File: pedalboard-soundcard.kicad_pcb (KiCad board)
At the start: 2 copper layers, 65 x 56 mm, 76 parts, among them J1 RPi_GPIO, J2 Conn_02x03_Odd_Even, J3 Conn_02x03_Odd_Even, U1 AT24CS01-STUM, U2 ncp163, U3 ncp163, U4 PCM1863DBT, U5 ncp163, U6 PCM5242RHBR, X1 22.5792Mhz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

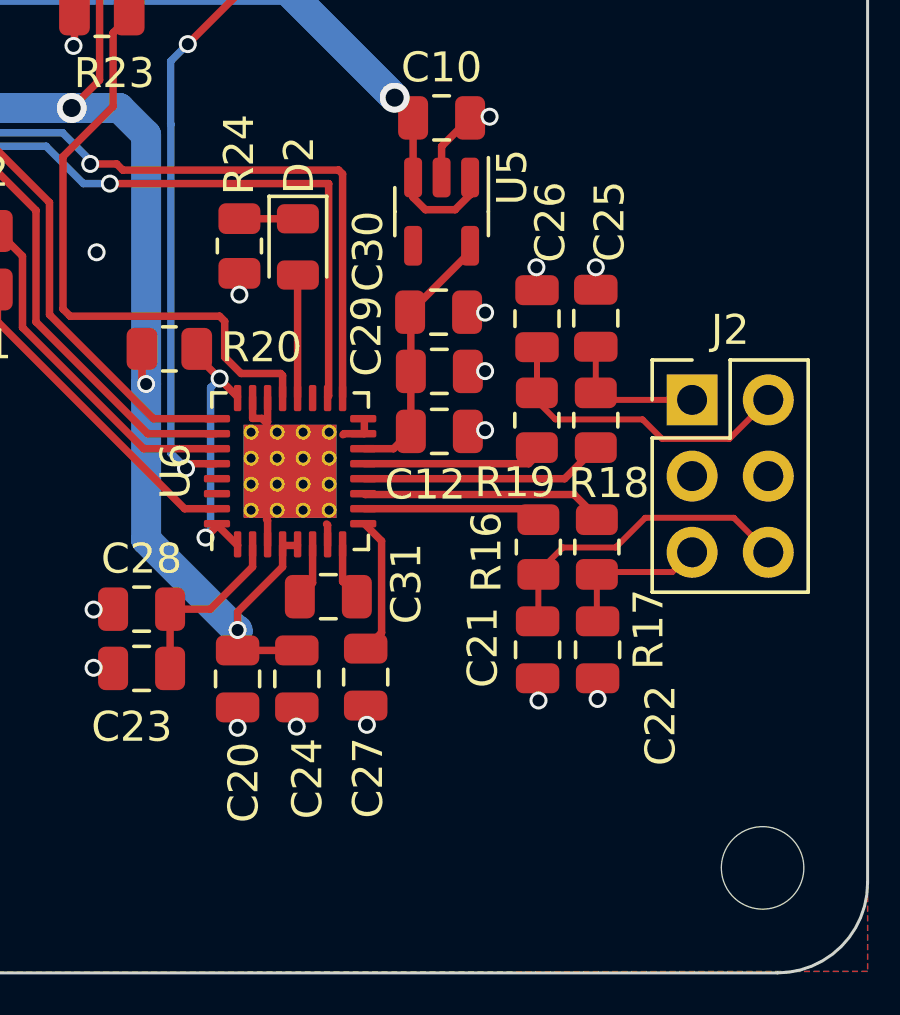
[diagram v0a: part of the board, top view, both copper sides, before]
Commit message: Cleanup silkscreen
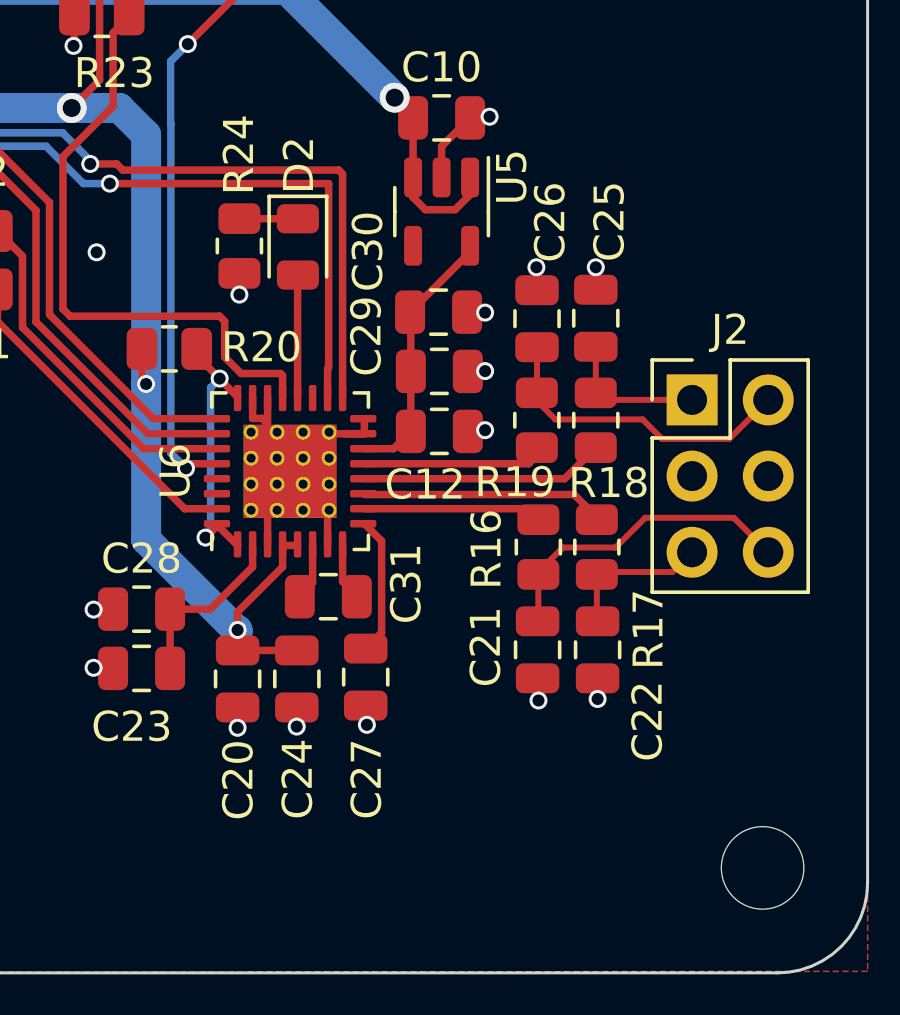
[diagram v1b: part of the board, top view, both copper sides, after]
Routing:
- net GND: track 56.3 -> 62.8 mm
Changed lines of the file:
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@@
     (property "ki_keywords" "mounting hole")
     (attr through_hole)
-    (fp_text reference "H4" (at 0 -4.0005) (layer "F.SilkS") hide
+    (fp_text reference "H4" (at 1.63 4.79) (layer "F.SilkS") hide
         (effects (font (size 1 1) (thickness 0.15)))
     )
@@
     (property "ki_keywords" "cap capacitor")
     (attr smd)
-    (fp_text reference "C21" (at -0.08 1.825 90) (layer "F.SilkS")
+    (fp_text reference "C21" (at -0.1 1.72 90) (layer "F.SilkS")
         (effects (font (size 1 1) (thickness 0.15)))
     )
@@
     (property "ki_keywords" "R res resistor")
     (attr smd)
-    (fp_text reference "R16" (at 0.17 1.725 90) (layer "F.SilkS")
+    (fp_text reference "R16" (at 0.075 1.725 90) (layer "F.SilkS")
         (effects (font (size 1 1) (thickness 0.15)))
     )
@@
     (property "ki_keywords" "cap capacitor")
     (attr smd)
-    (fp_text reference "C24" (at -3.325 0.35 90) (layer "F.SilkS")
+    (fp_text reference "C24" (at -3.34 0.035 90) (layer "F.SilkS")
         (effects (font (size 1 1) (thickness 0.15)))
     )
@@
     (property "ki_keywords" "cap capacitor")
     (attr smd)
-    (fp_text reference "C22" (at 2.52 -2.1 90) (layer "F.SilkS")
+    (fp_text reference "C22" (at 2.38 -1.67 90) (layer "F.SilkS")
         (effects (font (size 1 1) (thickness 0.15)))
     )
@@
     (property "ki_keywords" "cap capacitor")
     (attr smd)
-    (fp_text reference "C27" (at -3.36 0.08 90) (layer "F.SilkS")
+    (fp_text reference "C27" (at -3.4 0.04 90) (layer "F.SilkS")
         (effects (font (size 1 1) (thickness 0.15)))
     )
@@
     (property "ki_keywords" "cap capacitor")
     (attr smd)
-    (fp_text reference "C20" (at -3.45 0.2 90) (layer "F.SilkS")
+    (fp_text reference "C20" (at -3.37 0.03 90) (layer "F.SilkS")
         (effects (font (size 1 1) (thickness 0.15)))
     )
@@
   )
   (segment (start 66.650001 81.749999) (end 66.65 81.75) (width 0.25) (layer "F.Cu") (net 2))
+  (segment (start 93.499999 94.251999) (end 93.499999 92.527001) (width 0.25) (layer "F.Cu") (net 2))
   (segment (start 66.650001 79.249999) (end 66.65 79.25) (width 0.25) (layer "F.Cu") (net 2))
   (segment (start 88.35 96.375) (end 87.715 96.375) (width 0.25) (layer "F.Cu") (net 2))
@@
   (segment (start 96.724999 90.026559) (end 96.724999 90.526685) (width 0.25) (layer "F.Cu") (net 2))
   (segment (start 104.5 98.68) (end 104.5 99.37) (width 0.25) (layer "F.Cu") (net 2))
-  (segment (start 95.5 94.251999) (end 95.5 93.572099) (width 0.25) (layer "F.Cu") (net 2))
   (segment (start 82.84 61.15) (end 83.07 60.92) (width 0.25) (layer "F.Cu") (net 2))
   (segment (start 100.86 80) (end 100.9 79.96) (width 0.25) (layer "F.Cu") (net 2))
@@
   (segment (start 82.85 61.825) (end 82.85 61.16) (width 0.25) (layer "F.Cu") (net 2))
   (segment (start 67.4 61.725) (end 66.35 60.675) (width 0.25) (layer "F.Cu") (net 2))
-  (segment (start 95.5 93.572099) (end 95.465001 93.5371) (width 0.25) (layer "F.Cu") (net 2))
   (segment (start 94.475 100.285) (end 94.47 100.29) (width 0.01) (layer "F.Cu") (net 2))
   (segment (start 73.95 75.4) (end 73.95 74.65) (width 0.25) (layer "F.Cu") (net 2))
   (segment (start 93.4626 90.17077) (end 93.499999 90.133371) (width 0.25) (layer "F.Cu") (net 2))
-  (segment (start 93.499999 94.251999) (end 93.499999 93.420629) (width 0.25) (layer "F.Cu") (net 2))
   (segment (start 87.715 96.375) (end 87.7 96.39) (width 0.25) (layer "F.Cu") (net 2))
   (segment (start 100.175 90.45) (end 100.71 90.45) (width 0.25) (layer "F.Cu") (net 2))
@@
   (segment (start 100.74 88.45) (end 100.75 88.44) (width 0.25) (layer "F.Cu") (net 2))
   (segment (start 96.81 100.23) (end 96.77 100.19) (width 0.25) (layer "F.Cu") (net 2))
-  (segment (start 96.045226 90.526685) (end 96.0101 90.561811) (width 0.25) (layer "F.Cu") (net 2))
   (segment (start 62.150052 82.250001) (end 63.5 82.25) (width 0.25) (layer "F.Cu") (net 2))
   (segment (start 96.724999 90.526685) (end 96.045226 90.526685) (width 0.25) (layer "F.Cu") (net 2))
+  (segment (start 96.6875 90.527) (end 95.5 90.527) (width 0.25) (layer "F.Cu") (net 2))
   (segment (start 59.3925 77.0175) (end 59.42 76.99) (width 0.25) (layer "F.Cu") (net 2))
   (segment (start 102.46 84.98) (end 102.48 85) (width 0.25) (layer "F.Cu") (net 2))
@@
   (segment (start 88.75 72.62) (end 88.75 73.15) (width 0.25) (layer "F.Cu") (net 2))
   (segment (start 71.475 97.525) (end 71.47 97.53) (width 0.25) (layer "F.Cu") (net 2))
+  (segment (start 93.499999 92.527001) (end 94.25 91.777) (width 0.25) (layer "F.Cu") (net 2))
   (segment (start 63.349999 80.750001) (end 62.150052 80.750001) (width 0.25) (layer "F.Cu") (net 2))
   (segment (start 100.175 88.45) (end 100.74 88.45) (width 0.25) (layer "F.Cu") (net 2))
@@
   (segment (start 64.3 74.35) (end 64.3 73.65) (width 0.25) (layer "F.Cu") (net 2))
   (segment (start 100.15 86.475) (end 100.735 86.475) (width 0.25) (layer "F.Cu") (net 2))
+  (segment (start 95.5 93.027) (end 94.683333 92.210333) (width 0.25) (layer "F.Cu") (net 2))
   (segment (start 86.04 61.245001) (end 86.04 62.4775) (width 0.25) (layer "F.Cu") (net 2))
   (segment (start 87.1375 63.575) (end 87.1375 64.4225) (width 0.25) (layer "F.Cu") (net 2))
@@
   (segment (start 100.735 86.475) (end 100.75 86.49) (width 0.25) (layer "F.Cu") (net 2))
   (segment (start 58.1 96.7625) (end 58.1 97.46) (width 0.25) (layer "F.Cu") (net 2))
+  (segment (start 95.5 94.251999) (end 95.5 93.027) (width 0.25) (layer "F.Cu") (net 2))
   (segment (start 86.04 62.4775) (end 87.1375 63.575) (width 0.25) (layer "F.Cu") (net 2))
   (segment (start 94.475 99.65) (end 94.475 100.285) (width 0.01) (layer "F.Cu") (net 2))
@@
   (segment (start 63.5 82.75) (end 62.150052 82.75) (width 0.25) (layer "F.Cu") (net 2))
   (segment (start 102.48 85) (end 102.48 85.7425) (width 0.25) (layer "F.Cu") (net 2))
+  (segment (start 95.5 90.527) (end 94.25 91.777) (width 0.25) (layer "F.Cu") (net 2))
   (segment (start 73.45 96.8625) (end 73.45 97.52) (width 0.25) (layer "F.Cu") (net 2))
   (segment (start 87.0625 76.625) (end 87.0625 77.5675) (width 0.25) (layer "F.Cu") (net 2))
@@
   (segment (start 67.4 62.7125) (end 67.4 61.725) (width 0.25) (layer "F.Cu") (net 2))
   (segment (start 84.225 72.375) (end 84.225 73.0875) (width 0.01) (layer "F.Cu") (net 2))
-  (segment (start 93.499999 93.420629) (end 93.4626 93.38323) (width 0.25) (layer "F.Cu") (net 2))
   (segment (start 82.525 73.225) (end 82.525 72.695) (width 0.25) (layer "F.Cu") (net 2))
   (segment (start 96.77 100.19) (end 96.77 99.59) (width 0.25) (layer "F.Cu") (net 2))
@@
   (segment (start 66.103606 80.1195) (end 66.453606 80.4695) (width 0.25) (layer "B.Cu") (net 47))
   (segment (start 60.71 56.03) (end 61.95 57.27) (width 0.25) (layer "F.Cu") (net 48))
-  (segment (start 88.24 82.19) (end 95.53 82.19) (width 0.25) (layer "F.Cu") (net 48))
   (segment (start 65.844722 80.7445) (end 65.789384 80.7445) (width 0.25) (layer "F.Cu") (net 48))
+  (segment (start 95.535 82.195) (end 95.535 88.315) (width 0.25) (layer "F.Cu") (net 48))
+  (segment (start 95.5 88.35) (end 95.5 89.302001) (width 0.25) (layer "F.Cu") (net 48))
+  (segment (start 95.535 88.315) (end 95.5 88.35) (width 0.25) (layer "F.Cu") (net 48))
   (segment (start 56.1 77.113604) (end 58.2214 74.992204) (width 0.25) (layer "F.Cu") (net 48))
-  (segment (start 95.535 89.267001) (end 95.5 89.302001) (width 0.25) (layer "F.Cu") (net 48))
   (segment (start 64.783882 81.750002) (end 56.793606 81.750002) (width 0.25) (layer "F.Cu") (net 48))
-  (segment (start 95.535 82.195) (end 95.535 89.267001) (width 0.25) (layer "F.Cu") (net 48))
+  (segment (start 88.24 82.19) (end 95.53 82.19) (width 0.25) (layer "F.Cu") (net 48))
   (segment (start 56.1 81.056396) (end 56.1 77.113604) (width 0.25) (layer "F.Cu") (net 48))
   (segment (start 65.789384 80.7445) (end 64.783882 81.750002) (width 0.25) (layer "F.Cu") (net 48))
-  (segment (start 95.53 82.19) (end 95.535 82.195) (width 0.25) (layer "F.Cu") (net 48))
   (segment (start 56.793606 81.750002) (end 56.1 81.056396) (width 0.25) (layer "F.Cu") (net 48))
+  (segment (start 95.53 82.19) (end 95.535 82.195) (width 0.25) (layer "F.Cu") (net 48))
   (segment (start 58.2214 74.992204) (end 58.2214 56.614865) (width 0.25) (layer "F.Cu") (net 48))
   (segment (start 58.2214 56.614865) (end 58.806265 56.03) (width 0.25) (layer "F.Cu") (net 48))

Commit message: PCB text
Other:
- board text added: "${TITLE} ${COMPANY} PCB: ${REVISION}"
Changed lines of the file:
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@@
   (gr_line (start 49.5 89) (end 52.5 89)
     (stroke (width 0.1) (type solid)) (layer "Edge.Cuts"))
+  (gr_text "${TITLE}\n${COMPANY}\nPCB: ${REVISION}" (at 91.26 69.92) (layer "F.SilkS")
+    (effects (font (size 1 1) (thickness 0.15)) (justify left bottom))
+  )
   (gr_text "Dimensions taken from\nhttps://github.com/raspberrypi/hats/blob/master/hat-board-mechanical.pdf" (at 85 119) (layer "Cmts.User")
     (effects (font (size 1.5 1.5) (thickness 0.15) italic))

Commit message: Update from schematics
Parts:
- C1, C11, C19, C28, C32: value 100nf25v -> 100nF25V
- C10, C12, C15, C2, C3, C4, C5, C6, C7, C8, C9: value 10uf16v -> 10uF16V
- C13, C17, C18, C23, C30: value 1uf16v -> 1uF16V
- C14: value 100nf25V -> 100nF25V
- C16, C29: value 100nf16v -> 100nF25V
- C21, C22, C25, C26: value 2,2nf50v -> 2,2nF50V
- C24: value 1uf16V -> 1uF16V
- C27, C31: value 1uf 16v -> 1uF16V
- R1, R20, R23, R24, R25: value 10k -> 10K
- R10, R5, R6, R7: value 3K8 -> 3K9
- U2, U3, U5: value ncp163 -> NCP163

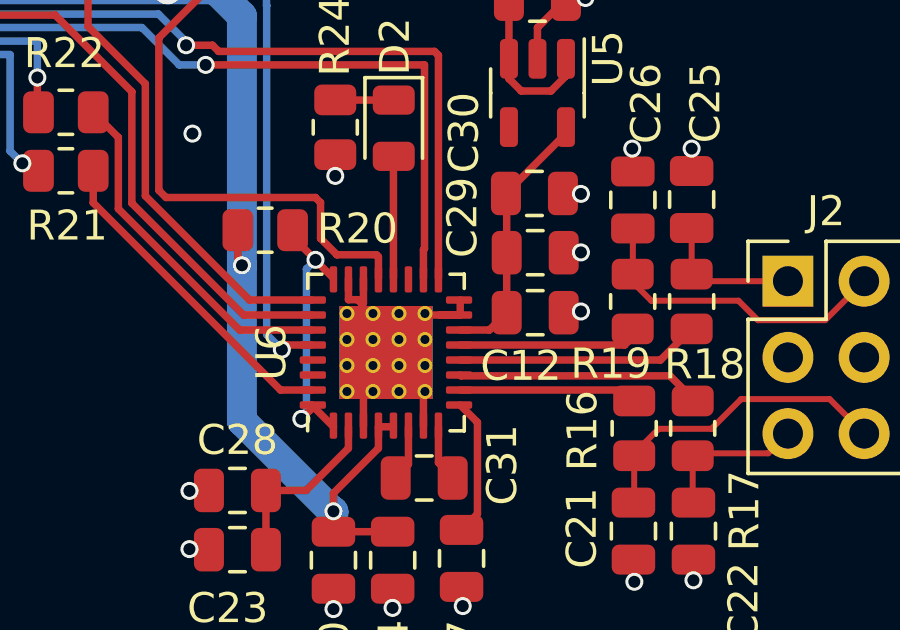
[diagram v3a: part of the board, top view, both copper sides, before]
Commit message: Cleanup schematic for eeprom
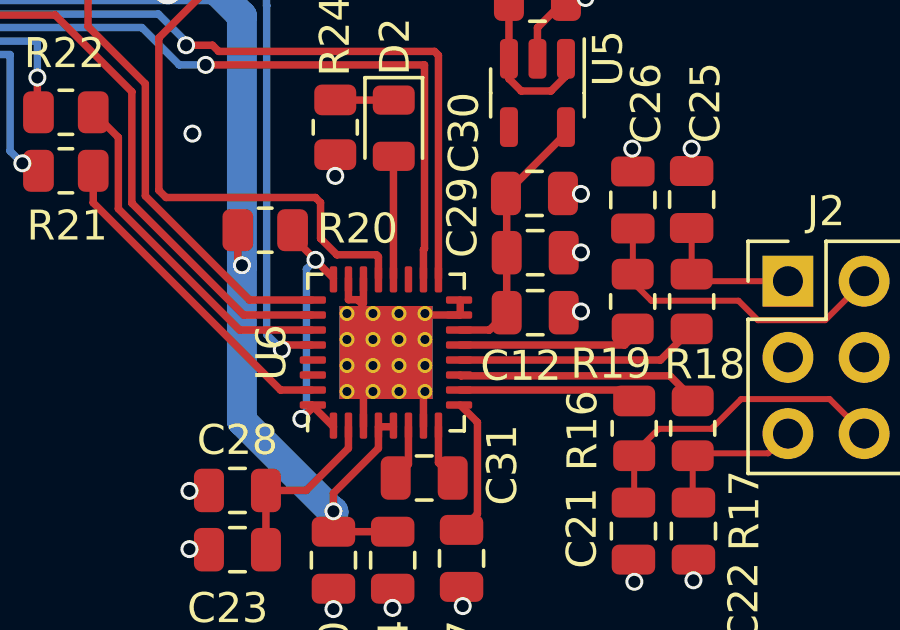
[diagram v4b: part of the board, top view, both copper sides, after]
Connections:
- net ID_SC renamed /ID_SC
- net ID_SD renamed /ID_SD
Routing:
- net GND: track 62.8 -> 62.1 mm
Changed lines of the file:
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@@
   (net 48 "scl")
   (net 49 "pcm_clk")
-  (net 50 "ID_SD")
-  (net 51 "ID_SC")
+  (net 50 "/ID_SD")
+  (net 51 "/ID_SC")
   (net 52 "pcm_fs")
   (net 53 "DOUT")
@@
       (net 26 "unconnected-(J1-BCM7_CE1-Pad26)") (pinfunction "BCM7_CE1") (pintype "bidirectional+no_connect"))
     (pad "27" thru_hole oval locked (at -1.27 8.89 90) (size 1.7272 1.7272) (drill 1.016) (layers "*.Cu" "*.Mask")
-      (net 50 "ID_SD") (pinfunction "BCM0_ID_SD") (pintype "bidirectional"))
+      (net 50 "/ID_SD") (pinfunction "BCM0_ID_SD") (pintype "bidirectional"))
     (pad "28" thru_hole oval locked (at 1.27 8.89 90) (size 1.7272 1.7272) (drill 1.016) (layers "*.Cu" "*.Mask")
-      (net 51 "ID_SC") (pinfunction "BCM1_ID_SC") (pintype "bidirectional"))
+      (net 51 "/ID_SC") (pinfunction "BCM1_ID_SC") (pintype "bidirectional"))
     (pad "29" thru_hole oval locked (at -1.27 11.43 90) (size 1.7272 1.7272) (drill 1.016) (layers "*.Cu" "*.Mask")
       (net 29 "unconnected-(J1-BCM5-Pad29)") (pinfunction "BCM5") (pintype "bidirectional+no_connect"))
@@
       (stroke (width 0.1) (type solid)) (layer "F.Fab"))
     (pad "1" smd roundrect (at -0.9125 0) (size 1.025 1.4) (layers "F.Cu" "F.Paste" "F.Mask") (roundrect_rratio 0.243902)
-      (net 51 "ID_SC") (pintype "passive"))
+      (net 51 "/ID_SC") (pintype "passive"))
     (pad "2" smd roundrect (at 0.9125 0) (size 1.025 1.4) (layers "F.Cu" "F.Paste" "F.Mask") (roundrect_rratio 0.243902)
       (net 3 "DVDD") (pintype "passive"))
@@
       (stroke (width 0.1) (type solid)) (layer "F.Fab"))
     (pad "1" smd roundrect (at -0.9125 0) (size 1.025 1.4) (layers "F.Cu" "F.Paste" "F.Mask") (roundrect_rratio 0.243902)
-      (net 50 "ID_SD") (pintype "passive"))
+      (net 50 "/ID_SD") (pintype "passive"))
     (pad "2" smd roundrect (at 0.9125 0) (size 1.025 1.4) (layers "F.Cu" "F.Paste" "F.Mask") (roundrect_rratio 0.243902)
       (net 3 "DVDD") (pintype "passive"))
@@
       (stroke (width 0.1) (type solid)) (layer "F.Fab"))
     (pad "1" smd roundrect (at -1.1375 -0.95 180) (size 1.325 0.6) (layers "F.Cu" "F.Paste" "F.Mask") (roundrect_rratio 0.25)
-      (net 51 "ID_SC") (pinfunction "SCL") (pintype "input"))
+      (net 51 "/ID_SC") (pinfunction "SCL") (pintype "input"))
     (pad "2" smd roundrect (at -1.1375 0 180) (size 1.325 0.6) (layers "F.Cu" "F.Paste" "F.Mask") (roundrect_rratio 0.25)
       (net 2 "GND") (pinfunction "GND") (pintype "power_in"))
     (pad "3" smd roundrect (at -1.1375 0.95 180) (size 1.325 0.6) (layers "F.Cu" "F.Paste" "F.Mask") (roundrect_rratio 0.25)
-      (net 50 "ID_SD") (pinfunction "SDA") (pintype "bidirectional"))
+      (net 50 "/ID_SD") (pinfunction "SDA") (pintype "bidirectional"))
     (pad "4" smd roundrect (at 1.1375 0.95 180) (size 1.325 0.6) (layers "F.Cu" "F.Paste" "F.Mask") (roundrect_rratio 0.25)
       (net 3 "DVDD") (pinfunction "VCC") (pintype "power_in"))
@@
   (segment (start 96.81 100.23) (end 96.77 100.19) (width 0.25) (layer "F.Cu") (net 2))
   (segment (start 62.150052 82.250001) (end 63.5 82.25) (width 0.25) (layer "F.Cu") (net 2))
-  (segment (start 96.724999 90.526685) (end 96.045226 90.526685) (width 0.25) (layer "F.Cu") (net 2))
   (segment (start 96.6875 90.527) (end 95.5 90.527) (width 0.25) (layer "F.Cu") (net 2))
   (segment (start 59.3925 77.0175) (end 59.42 76.99) (width 0.25) (layer "F.Cu") (net 2))
